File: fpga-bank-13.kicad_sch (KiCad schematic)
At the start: 1 part

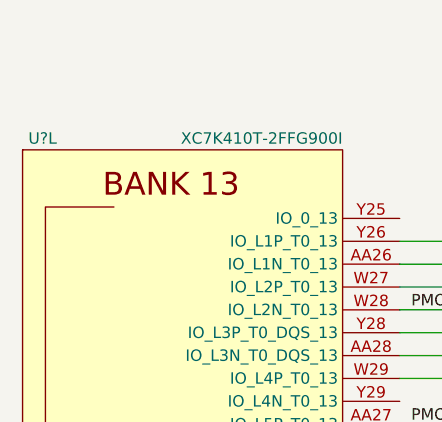
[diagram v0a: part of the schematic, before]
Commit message: Fix FPGA symbol
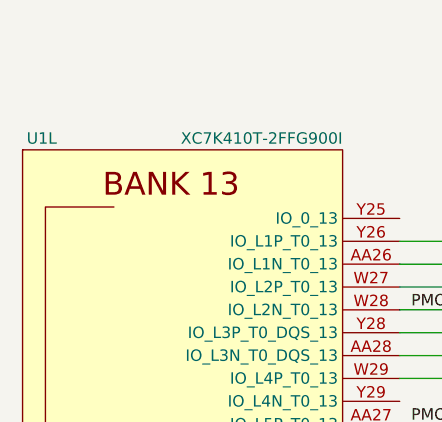
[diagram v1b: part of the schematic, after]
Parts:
- gave numbers to parts that had none: 1
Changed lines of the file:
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@@
     (effects (font (size 1.27 1.27)) (justify left))
   )
-  (symbol (lib_name "XC7K410T-2FFG900I_1") (lib_id "antmicroMicrocontrollers:XC7K410T-2FFG900I") (at 119.38 144.78 0) (unit 12)
+  (symbol (lib_id "antmicroMicrocontrollers:XC7K410T-2FFG900I") (at 119.38 144.78 0) (unit 12)
     (in_bom yes) (on_board yes)
-    (property "Reference" "U?" (id 0) (at 105.41 74.93 0)
+    (property "Reference" "U1" (id 0) (at 105.41 74.93 0)
       (effects (font (size 1.27 1.27)) (justify right))
     )

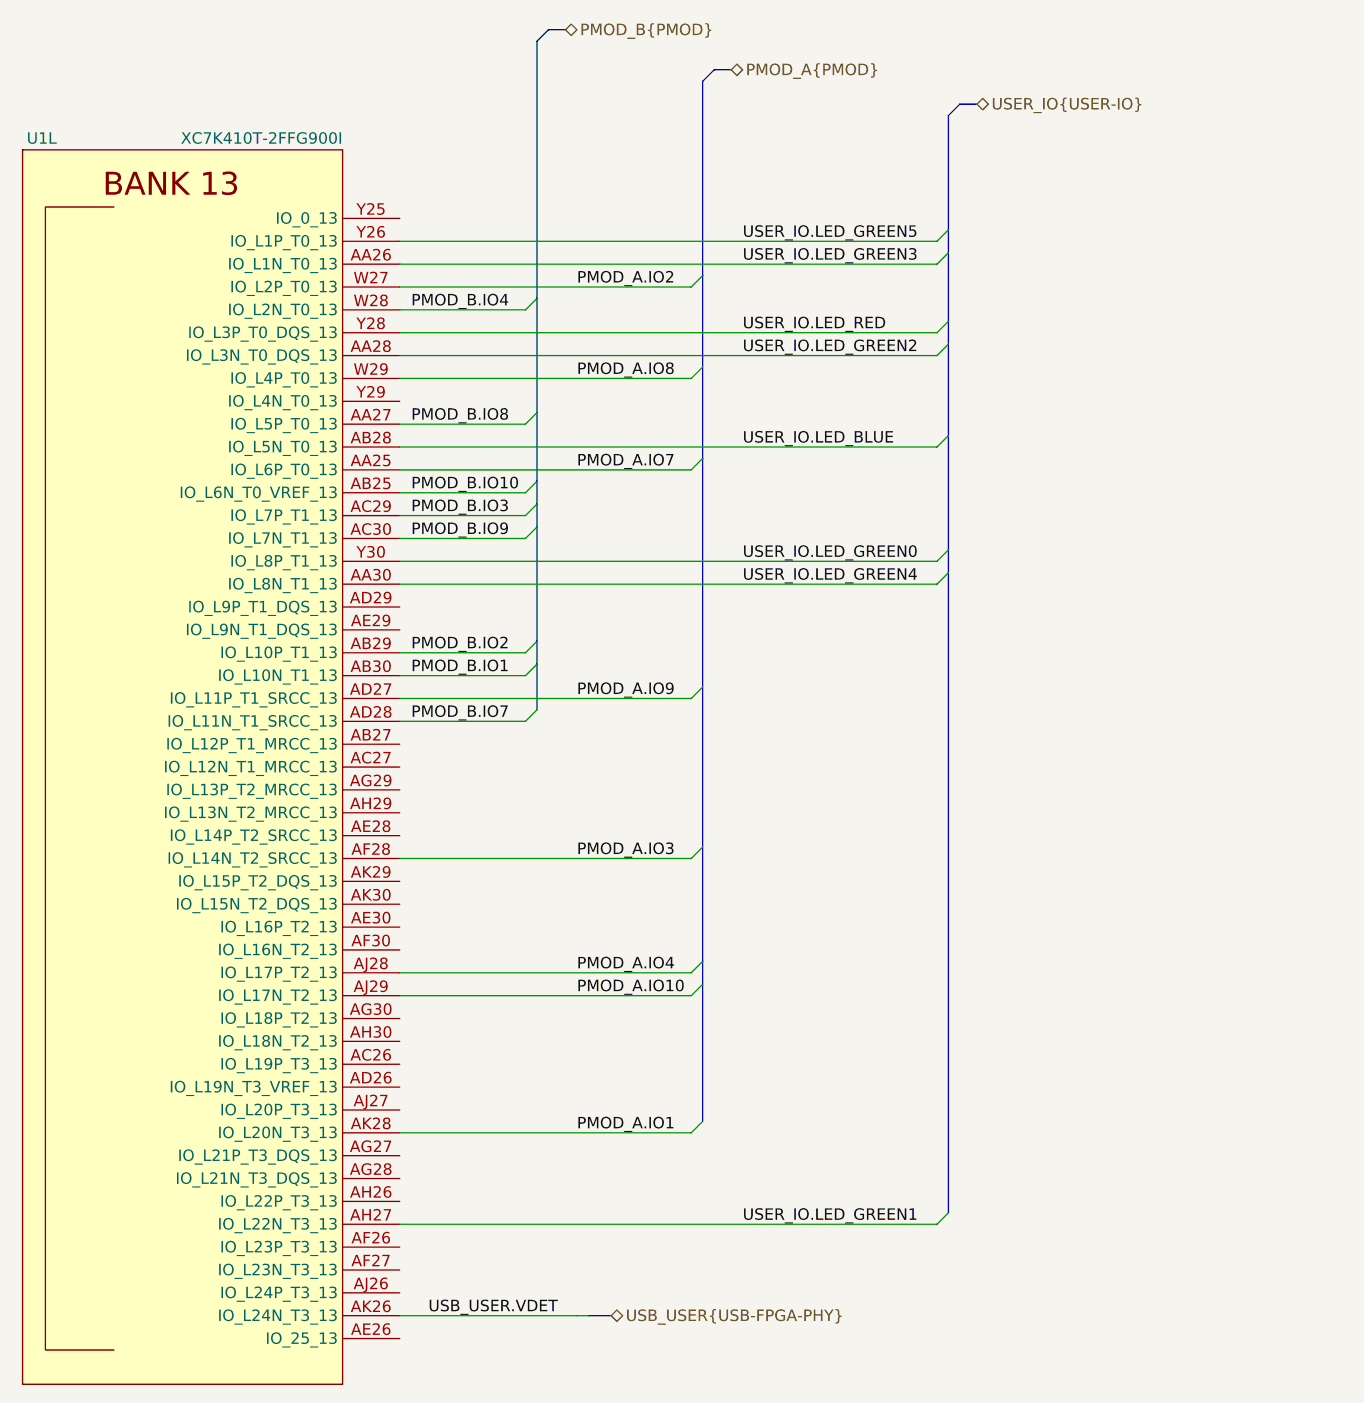
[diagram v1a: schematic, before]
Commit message: Connect I2C bus
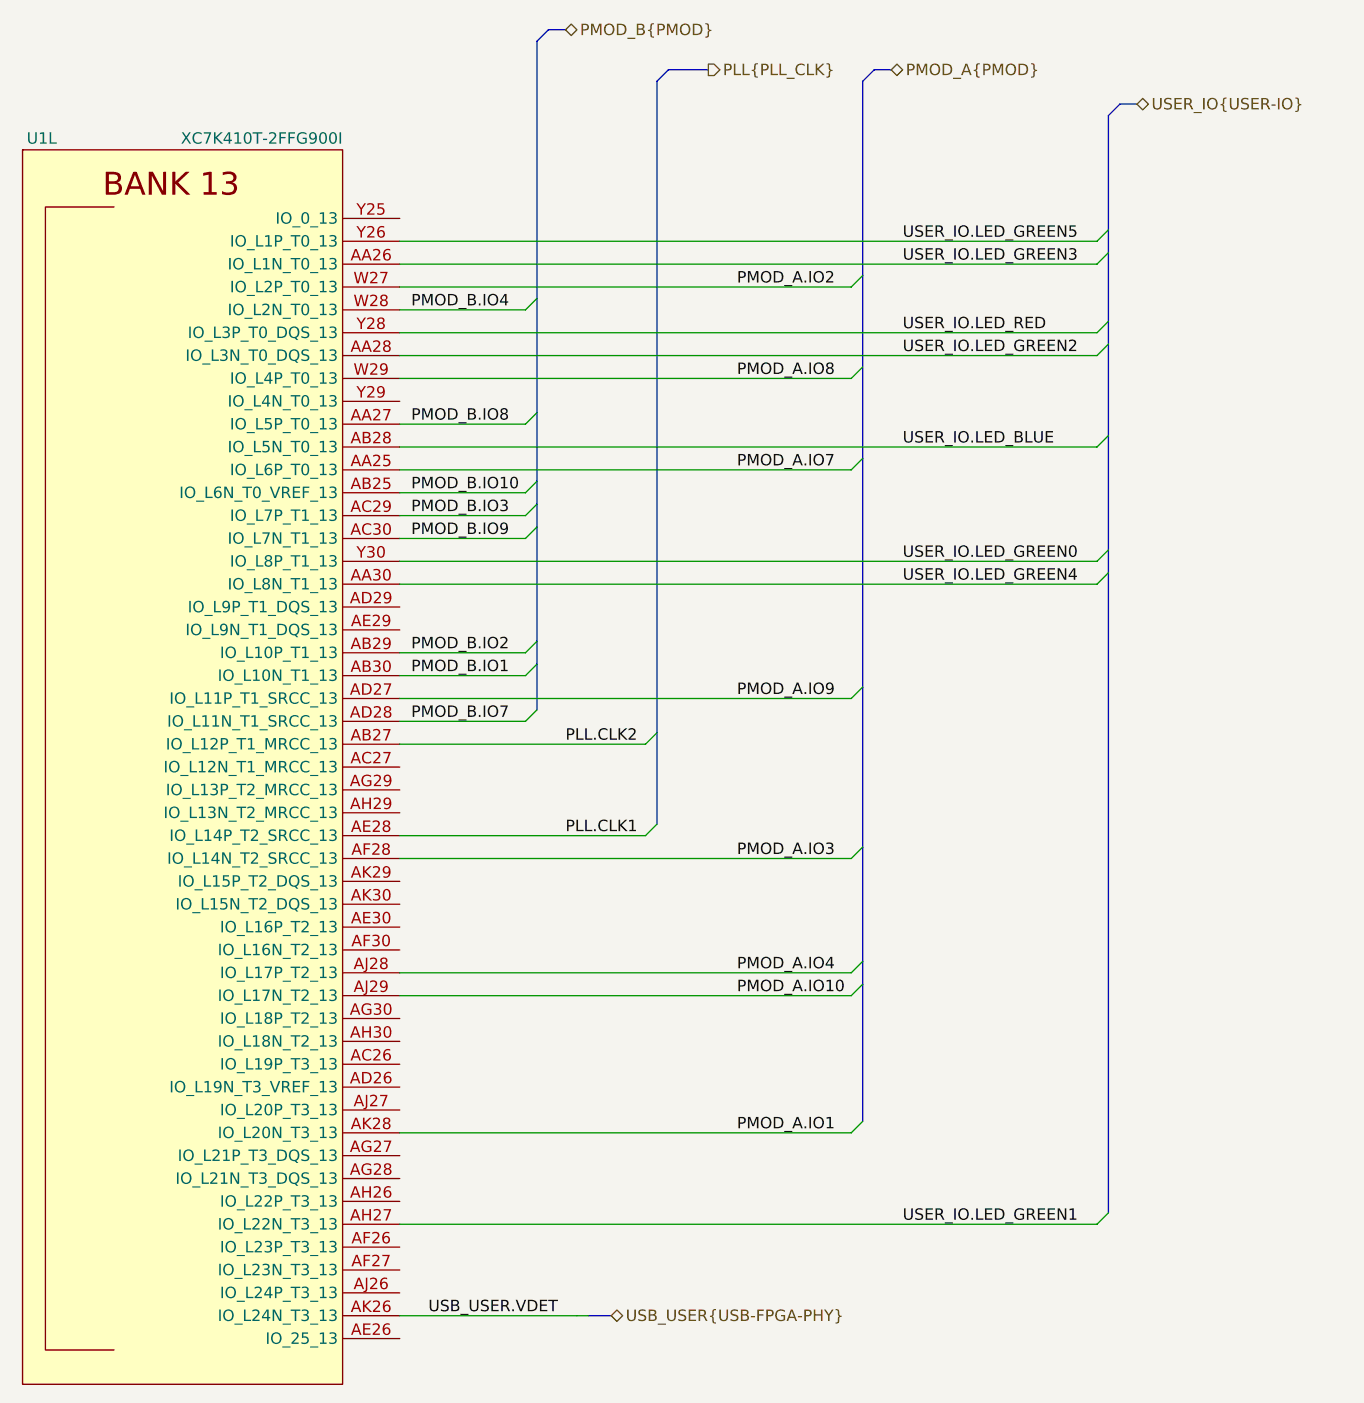
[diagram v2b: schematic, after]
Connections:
- net PLL.CLK2: now reaches U1.AB27 (IO_L12P_T1_MRCC_13)
- net PLL.CLK1: now reaches U1.AE28 (IO_L14P_T2_SRCC_13)

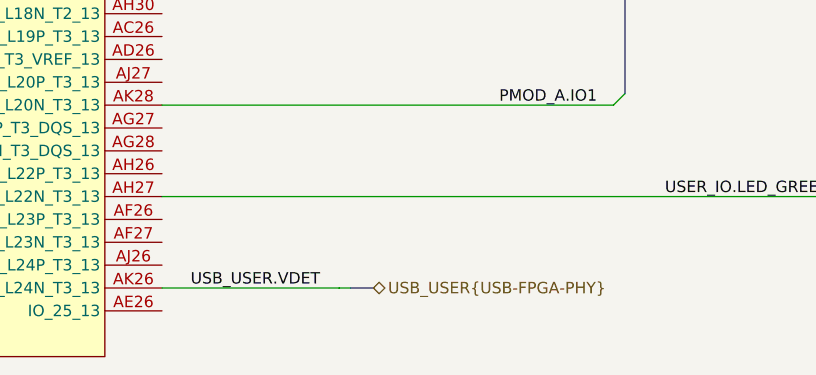
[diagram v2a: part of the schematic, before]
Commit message: Connect USB_HOST on root schematic
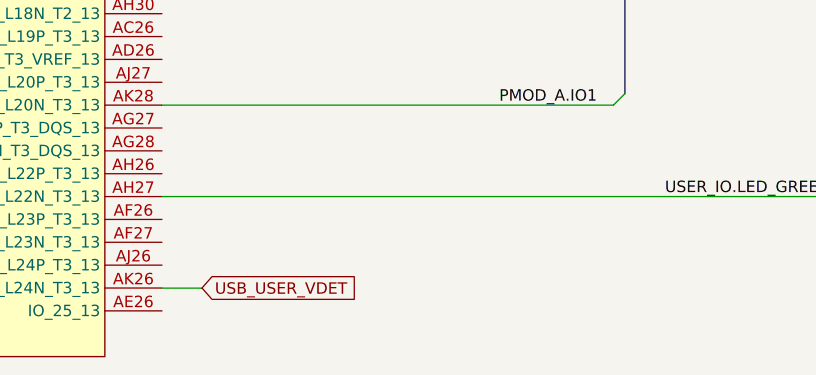
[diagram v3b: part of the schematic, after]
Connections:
- net USB_USER.VDET renamed USB_USER_VDET
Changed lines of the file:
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@@
-    (stroke (width 0) (type default) (color 0 0 0 0))
-  )
-  (bus_entry (at 163.195 205.74) (size 1.27 0)
     (stroke (width 0) (type default) (color 0 0 0 0))
   )
@@
     (stroke (width 0) (type default) (color 0 0 0 0))
   )
+  (wire (pts (xy 147.955 205.74) (xy 143.51 205.74))
+    (stroke (width 0) (type default) (color 0 0 0 0))
+  )
   (wire (pts (xy 143.51 139.7) (xy 157.48 139.7))
     (stroke (width 0) (type default) (color 0 0 0 0))
@@
     (stroke (width 0) (type default) (color 0 0 0 0))
   )
-  (bus (pts (xy 164.465 205.74) (xy 167.005 205.74))
-    (stroke (width 0) (type default) (color 0 0 0 0))
-  )
   (wire (pts (xy 143.51 106.68) (xy 157.48 106.68))
     (stroke (width 0) (type default) (color 0 0 0 0))
@@
     (stroke (width 0) (type default) (color 0 0 0 0))
   )
-  (wire (pts (xy 163.195 205.74) (xy 143.51 205.74))
-    (stroke (width 0) (type default) (color 0 0 0 0))
-  )
   (wire (pts (xy 143.51 116.84) (xy 157.48 116.84))
     (stroke (width 0) (type default) (color 0 0 0 0))
@@
     (effects (font (size 1.27 1.27)) (justify left bottom))
   )
-  (label "USB_USER.VDET" (at 146.685 205.74 0)
-    (effects (font (size 1.27 1.27)) (justify left bottom))
-  )
   (label "PMOD_A.IO1" (at 180.975 185.42 0)
     (effects (font (size 1.27 1.27)) (justify left bottom))
@@
   (label "PMOD_B.IO10" (at 144.78 114.3 0)
     (effects (font (size 1.27 1.27)) (justify left bottom))
+  )
+  (global_label "USB_USER_VDET" (shape input) (at 147.955 205.74 0) (fields_autoplaced)
+    (effects (font (size 1.27 1.27)) (justify left))
+    (property "Intersheet References" "${INTERSHEET_REFS}" (id 0) (at 165.5476 205.6606 0)
+      (effects (font (size 1.27 1.27)) (justify left) hide)
+    )
   )
   (hierarchical_label "PLL{PLL_CLK}" (shape output) (at 177.8 67.31 0)
     (effects (font (size 1.27 1.27)) (justify left))
   )
-  (hierarchical_label "USB_USER{USB-FPGA-PHY}" (shape bidirectional) (at 167.005 205.74 0)
-    (effects (font (size 1.27 1.27)) (justify left))
-  )

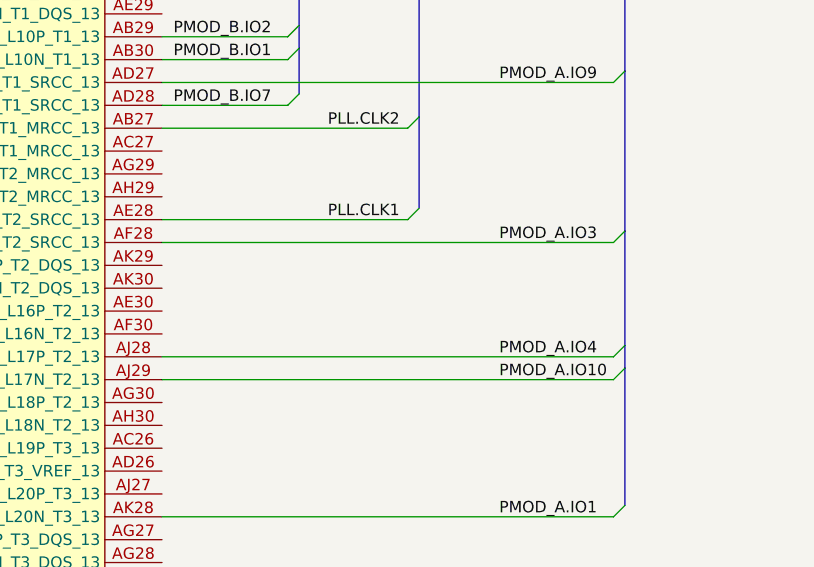
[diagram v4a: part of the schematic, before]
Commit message: Add new pinout to sup MCU. Start connecting it to FPGA
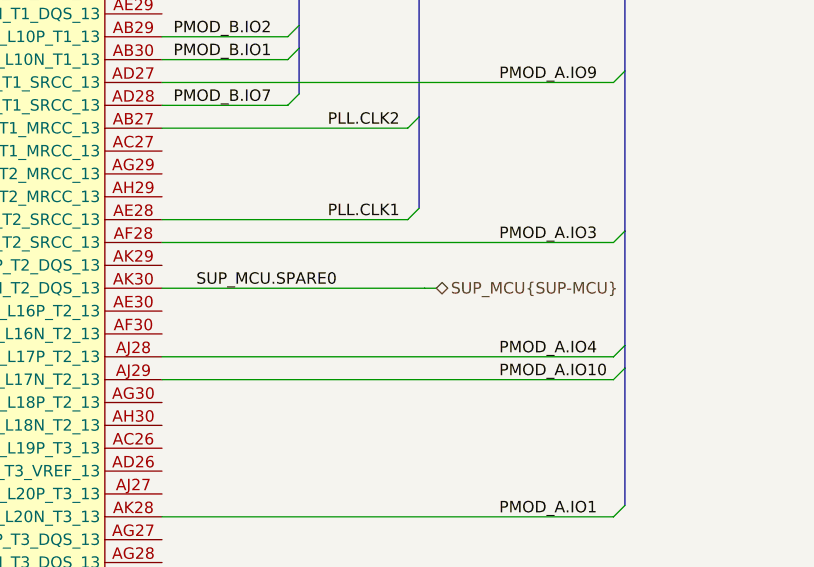
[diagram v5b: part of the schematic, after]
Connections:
- net SUP_MCU.SPARE0: now reaches U1.AK30 (IO_L15N_T2_DQS_13)
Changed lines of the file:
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@@
+    (stroke (width 0) (type default) (color 0 0 0 0))
+  )
+  (bus_entry (at 172.72 160.02) (size 1.27 0)
     (stroke (width 0) (type default) (color 0 0 0 0))
   )
@@
     (stroke (width 0) (type default) (color 0 0 0 0))
   )
+  (wire (pts (xy 143.51 160.02) (xy 172.72 160.02))
+    (stroke (width 0) (type default) (color 0 0 0 0))
+  )
   (wire (pts (xy 147.955 205.74) (xy 143.51 205.74))
     (stroke (width 0) (type default) (color 0 0 0 0))
@@
   )
   (label "PMOD_B.IO2" (at 144.78 132.08 0)
+    (effects (font (size 1.27 1.27)) (justify left bottom))
+  )
+  (label "SUP_MCU.SPARE0" (at 147.32 160.02 0)
     (effects (font (size 1.27 1.27)) (justify left bottom))
   )
@@
     )
   )
+  (hierarchical_label "SUP_MCU{SUP-MCU}" (shape bidirectional) (at 173.99 160.02 0)
+    (effects (font (size 1.27 1.27)) (justify left))
+  )
   (hierarchical_label "PLL{PLL_CLK}" (shape output) (at 177.8 67.31 0)

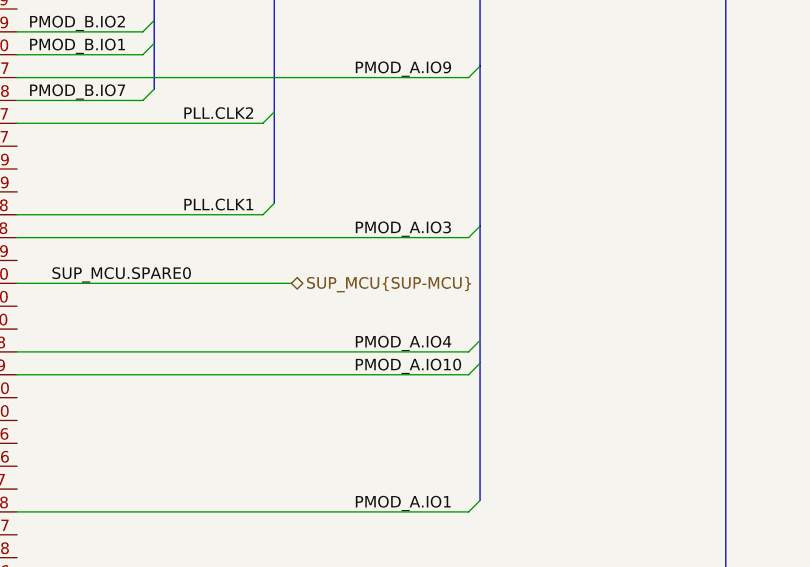
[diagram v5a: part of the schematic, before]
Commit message: Improve placement of the GBE and USB Host PHY. Update pinout for better routing
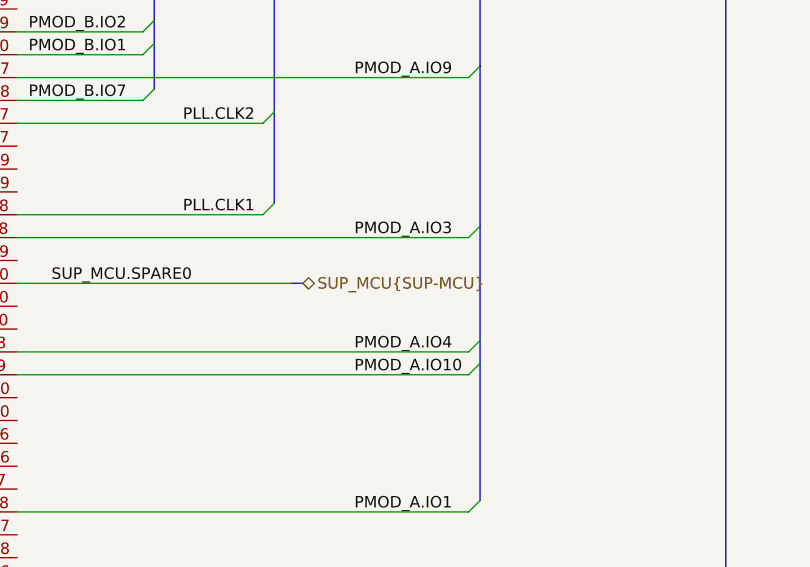
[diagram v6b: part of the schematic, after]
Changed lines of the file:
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@@
+    (stroke (width 0) (type default) (color 0 0 0 0))
+  )
+  (bus (pts (xy 173.99 160.02) (xy 175.26 160.02))
     (stroke (width 0) (type default) (color 0 0 0 0))
   )
@@
     )
   )
-  (hierarchical_label "SUP_MCU{SUP-MCU}" (shape bidirectional) (at 173.99 160.02 0)
+  (hierarchical_label "SUP_MCU{SUP-MCU}" (shape bidirectional) (at 175.26 160.02 0)
     (effects (font (size 1.27 1.27)) (justify left))
   )

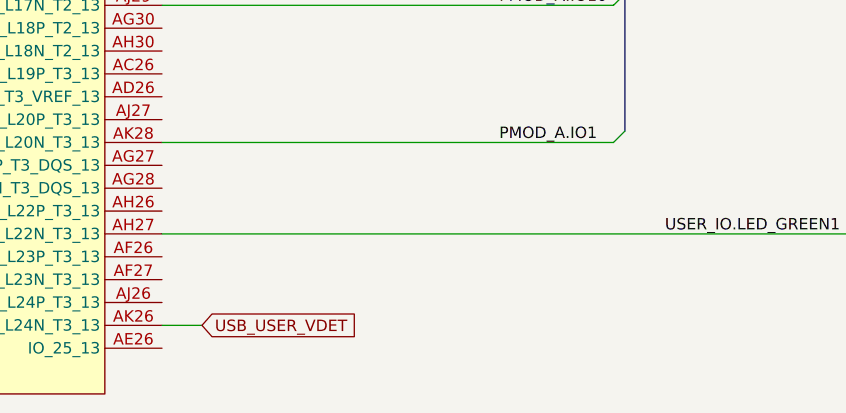
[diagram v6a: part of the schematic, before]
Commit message: Connected PB_CTRL_OUT and PB_CTRL_INT signals to FPGA
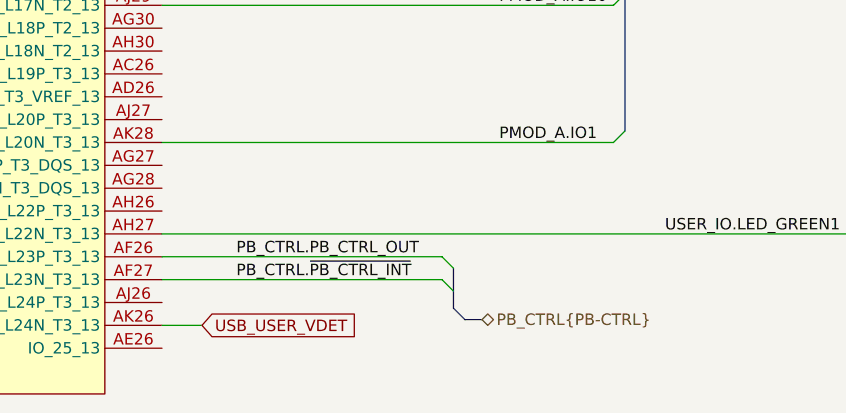
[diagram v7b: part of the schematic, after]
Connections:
- net PB_CTRL.PB_CTRL_OUT: now reaches U1.AF26 (IO_L23P_T3_13)
- net PB_CTRL.~{PB_CTRL_INT}: now reaches U1.AF27 (IO_L23N_T3_13)
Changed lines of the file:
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@@
     (rev "0.0.99")
   )
+  (bus_entry (at 175.895 201.93) (size -1.27 -1.27)
+    (stroke (width 0) (type default) (color 0 0 0 0))
+  )
   (bus_entry (at 194.945 184.15) (size -1.27 1.27)
     (stroke (width 0) (type default) (color 0 0 0 0))
@@
     (stroke (width 0) (type default) (color 0 0 0 0))
   )
+  (bus_entry (at 175.895 199.39) (size -1.27 -1.27)
+    (stroke (width 0) (type default) (color 0 0 0 0))
+  )
   (bus_entry (at 194.945 135.89) (size -1.27 1.27)
     (stroke (width 0) (type default) (color 0 0 0 0))
@@
     (stroke (width 0) (type default) (color 0 0 0 0))
   )
+  (bus (pts (xy 175.895 199.39) (xy 175.895 201.93))
+    (stroke (width 0) (type default) (color 0 0 0 0))
+  )
   (bus (pts (xy 222.25 97.79) (xy 222.25 95.25))
     (stroke (width 0) (type default) (color 0 0 0 0))
   )
+  (bus (pts (xy 175.895 201.93) (xy 175.895 203.835))
+    (stroke (width 0) (type default) (color 0 0 0 0))
+  )
   (wire (pts (xy 143.51 142.24) (xy 170.815 142.24))
     (stroke (width 0) (type default) (color 0 0 0 0))
@@
     (stroke (width 0) (type default) (color 0 0 0 0))
   )
+  (wire (pts (xy 143.51 198.12) (xy 174.625 198.12))
+    (stroke (width 0) (type default) (color 0 0 0 0))
+  )
   (bus (pts (xy 158.75 113.03) (xy 158.75 115.57))
     (stroke (width 0) (type default) (color 0 0 0 0))
@@
     (stroke (width 0) (type default) (color 0 0 0 0))
   )
+  (wire (pts (xy 143.51 200.66) (xy 174.625 200.66))
+    (stroke (width 0) (type default) (color 0 0 0 0))
+  )
   (bus (pts (xy 194.945 110.49) (xy 194.945 135.89))
     (stroke (width 0) (type default) (color 0 0 0 0))
@@
     (stroke (width 0) (type default) (color 0 0 0 0))
   )
+  (bus (pts (xy 175.895 203.835) (xy 177.165 205.105))
+    (stroke (width 0) (type default) (color 0 0 0 0))
+  )
   (bus (pts (xy 222.25 72.39) (xy 223.52 71.12))
     (stroke (width 0) (type default) (color 0 0 0 0))
@@
     (stroke (width 0) (type default) (color 0 0 0 0))
   )
+  (bus (pts (xy 179.07 205.105) (xy 177.165 205.105))
+    (stroke (width 0) (type default) (color 0 0 0 0))
+  )
   (wire (pts (xy 143.51 152.4) (xy 170.815 152.4))
     (stroke (width 0) (type default) (color 0 0 0 0))
@@
     (effects (font (size 1.27 1.27)) (justify left bottom))
   )
+  (label "PB_CTRL.PB_CTRL_OUT" (at 151.765 198.12 0)
+    (effects (font (size 1.27 1.27)) (justify left bottom))
+  )
   (label "PMOD_B.IO7" (at 144.78 139.7 0)
     (effects (font (size 1.27 1.27)) (justify left bottom))
@@
   )
   (label "PMOD_A.IO8" (at 180.975 101.6 0)
+    (effects (font (size 1.27 1.27)) (justify left bottom))
+  )
+  (label "PB_CTRL.~{PB_CTRL_INT}" (at 151.765 200.66 0)
     (effects (font (size 1.27 1.27)) (justify left bottom))
   )
@@
     (effects (font (size 1.27 1.27)) (justify left))
   )
+  (hierarchical_label "PB_CTRL{PB-CTRL}" (shape bidirectional) (at 179.07 205.105 0)
+    (effects (font (size 1.27 1.27)) (justify left))
+  )
